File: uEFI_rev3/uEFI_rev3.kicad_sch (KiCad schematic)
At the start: 89 parts, among them J1 USB_B, J2 Tag connect, J4 Conn_02x08_Odd_Even, J5 Conn_01x03, Q11 SS8050, Q12 AO3400A, Q13 AO3400A, Q8 SS8050, Q9 SS8050, SW1 SW_Push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

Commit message: uEFI r3.2
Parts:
- added C42: 100uF ±20% 35V, Capacitor_SMD:CP_Elec_6.3x7.7, symbol Device:CP_Small
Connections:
- net +12V: now also C42.1
- net GND: now also C42.2
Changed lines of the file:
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@@
     (stroke (width 0) (type solid) (color 0 0 0 0))
   )
+  (wire (pts (xy 163.83 40.005) (xy 163.83 41.275))
+    (stroke (width 0) (type default) (color 0 0 0 0))
+  )
   (wire (pts (xy 60.96 26.67) (xy 75.565 26.67))
     (stroke (width 0) (type solid) (color 0 0 0 0))
@@
     (stroke (width 0) (type solid) (color 0 0 0 0))
   )
+  (wire (pts (xy 163.83 46.355) (xy 163.83 50.165))
+    (stroke (width 0) (type default) (color 0 0 0 0))
+  )
   (wire (pts (xy 185.42 224.79) (xy 185.42 227.33))
     (stroke (width 0) (type solid) (color 0 0 0 0))
@@
     (pin "2")
   )
+  (symbol (lib_id "power:GND") (at 163.83 50.165 0) (unit 1)
+    (in_bom yes) (on_board yes)
+    (property "Reference" "#PWR070" (id 0) (at 163.83 56.515 0)
+      (effects (font (size 1.27 1.27)) hide)
+    )
+    (property "Value" "GND" (id 1) (at 163.9443 54.4894 0))
+    (property "Footprint" "" (id 2) (at 163.83 50.165 0)
+      (effects (font (size 1.27 1.27)) hide)
+    )
+    (property "Datasheet" "" (id 3) (at 163.83 50.165 0)
+      (effects (font (size 1.27 1.27)) hide)
+    )
+    (pin "1")
+  )
   (symbol (lib_id "Device:LED") (at 374.015 201.93 90) (unit 1)
     (in_bom yes) (on_board yes)
@@
     (pin "2")
   )
+  (symbol (lib_id "Device:CP_Small") (at 163.83 43.815 0) (unit 1)
+    (in_bom yes) (on_board yes)
+    (property "Reference" "C42" (id 0) (at 166.0652 42.6466 0)
+      (effects (font (size 1.27 1.27)) (justify left))
+    )
+    (property "Value" "100uF ±20% 35V" (id 1) (at 166.0652 44.958 0)
+      (effects (font (size 1.27 1.27)) (justify left))
+    )
+    (property "Footprint" "Capacitor_SMD:CP_Elec_6.3x7.7" (id 2) (at 163.83 43.815 0)
+      (effects (font (size 1.27 1.27)) hide)
+    )
+    (property "Datasheet" "~" (id 3) (at 163.83 43.815 0)
+      (effects (font (size 1.27 1.27)) hide)
+    )
+    (property "LCSC" "C141427" (id 4) (at 163.83 43.815 0)
+      (effects (font (size 0.889 0.889)) hide)
+    )
+    (pin "1")
+    (pin "2")
+  )
   (symbol (lib_id "Device:LED") (at 372.745 158.115 90) (unit 1)
     (in_bom yes) (on_board yes)
@@
     (pin "2")
   )
+  (symbol (lib_id "power:+12V") (at 163.83 40.005 0) (unit 1)
+    (in_bom yes) (on_board yes)
+    (property "Reference" "#PWR059" (id 0) (at 163.83 43.815 0)
+      (effects (font (size 1.27 1.27)) hide)
+    )
+    (property "Value" "+12V" (id 1) (at 164.1983 35.6806 0))
+    (property "Footprint" "" (id 2) (at 163.83 40.005 0)
+      (effects (font (size 1.27 1.27)) hide)
+    )
+    (property "Datasheet" "" (id 3) (at 163.83 40.005 0)
+      (effects (font (size 1.27 1.27)) hide)
+    )
+    (pin "1")
+  )
   (symbol (lib_id "Connector:TestPoint") (at 321.31 206.375 0) (unit 1)
     (in_bom yes) (on_board yes)
@@
       (reference "#PWR058") (unit 1) (value "GND") (footprint "")
     )
+    (path "/6a695035-302a-4633-872f-d86fe3f64f9b"
+      (reference "#PWR059") (unit 1) (value "+12V") (footprint "")
+    )
     (path "/00000000-0000-0000-0000-00005f54b134/6f9e6eea-f1a5-4e59-a7b8-03098e367ddb"
       (reference "#PWR060") (unit 1) (value "+5C") (footprint "")
@@
       (reference "#PWR069") (unit 1) (value "GNDA") (footprint "")
     )
+    (path "/0df50f59-0981-4c75-9182-aabf7e291901"
+      (reference "#PWR070") (unit 1) (value "GND") (footprint "")
+    )
     (path "/00000000-0000-0000-0000-00005f54b134/33b6552b-ec9a-44b7-995a-5c278ca4a586"
       (reference "#PWR071") (unit 1) (value "+5C") (footprint "")
@@
       (reference "C41") (unit 1) (value "0.01uF") (footprint "Capacitor_SMD:C_0805_2012Metric")
     )
+    (path "/1feee1ca-03cf-42e2-a7c2-0e718be37bce"
+      (reference "C42") (unit 1) (value "100uF ±20% 35V") (footprint "Capacitor_SMD:CP_Elec_6.3x7.7")
+    )
     (path "/00000000-0000-0000-0000-00005f54b134/00000000-0000-0000-0000-00006090d894"
       (reference "C49") (unit 1) (value "240pF") (footprint "Capacitor_SMD:C_0603_1608Metric")
@@
     )
     (path "/00000000-0000-0000-0000-00005f54b134/36d4577c-93b8-425e-bae5-ab676247b4dd"
-      (reference "D15") (unit 1) (value "K26") (footprint "Diode_SMD:D_SOD-123F")
+      (reference "D15") (unit 1) (value "K26") (footprint "Diode_SMD:D_SOD-323")
     )
     (path "/00000000-0000-0000-0000-00005f54b134/43df4a53-5a75-4543-88d3-50cd7393567d"
-      (reference "D16") (unit 1) (value "K26") (footprint "Diode_SMD:D_SOD-123F")
+      (reference "D16") (unit 1) (value "K26") (footprint "Diode_SMD:D_SOD-323")
     )
     (path "/00000000-0000-0000-0000-00005f54b134/3e35f35b-de57-42a1-b66b-690d937f1fec"
-      (reference "D17") (unit 1) (value "K26") (footprint "Diode_SMD:D_SOD-123F")
+      (reference "D17") (unit 1) (value "K26") (footprint "Diode_SMD:D_SOD-323")
     )
     (path "/00000000-0000-0000-0000-00005f54b134/78a824b0-87dc-437f-a732-d014d3bc51a5"
-      (reference "D18") (unit 1) (value "K26") (footprint "Diode_SMD:D_SOD-123F")
+      (reference "D18") (unit 1) (value "K26") (footprint "Diode_SMD:D_SOD-323")
     )
     (path "/00000000-0000-0000-0000-00005f54b134/961d11cf-9d35-4dc0-aeb1-54327f99e8be"
-      (reference "D19") (unit 1) (value "K26") (footprint "Diode_SMD:D_SOD-123F")
+      (reference "D19") (unit 1) (value "K26") (footprint "Diode_SMD:D_SOD-323")
     )
     (path "/00000000-0000-0000-0000-00005f54b134/21de7dcb-5425-42bb-8c9a-3bfd52b7a51a"
-      (reference "D20") (unit 1) (value "K26") (footprint "Diode_SMD:D_SOD-123F")
+      (reference "D20") (unit 1) (value "K26") (footprint "Diode_SMD:D_SOD-323")
     )
     (path "/00000000-0000-0000-0000-00005f54b134/2b82281b-f421-4ecf-b0db-00934e89dd91"
-      (reference "D21") (unit 1) (value "K26") (footprint "Diode_SMD:D_SOD-123F")
+      (reference "D21") (unit 1) (value "K26") (footprint "Diode_SMD:D_SOD-323")
     )
     (path "/00000000-0000-0000-0000-00005f54b134/eaa007a4-c036-46e7-bd00-a1283bc87d20"
-      (reference "D22") (unit 1) (value "K26") (footprint "Diode_SMD:D_SOD-123F")
+      (reference "D22") (unit 1) (value "K26") (footprint "Diode_SMD:D_SOD-323")
     )
     (path "/00000000-0000-0000-0000-00005f54b134/8d3f1cc5-e6e3-4ecd-92fe-e11a349d591c"
-      (reference "D23") (unit 1) (value "K26") (footprint "Diode_SMD:D_SOD-123F")
+      (reference "D23") (unit 1) (value "K26") (footprint "Diode_SMD:D_SOD-323")
     )
     (path "/00000000-0000-0000-0000-00005f54b134/36ef3d3a-8f83-46bb-b29a-eea3c6d5118e"
-      (reference "D24") (unit 1) (value "K26") (footprint "Diode_SMD:D_SOD-123F")
+      (reference "D24") (unit 1) (value "K26") (footprint "Diode_SMD:D_SOD-323")
     )
     (path "/00000000-0000-0000-0000-00005f54b134/e82e2f0c-57f5-4439-8e3d-91cef29bd2c9"
-      (reference "D25") (unit 1) (value "K26") (footprint "Diode_SMD:D_SOD-123F")
+      (reference "D25") (unit 1) (value "K26") (footprint "Diode_SMD:D_SOD-323")
     )
     (path "/00000000-0000-0000-0000-00005f54b134/81a46c04-d71f-4df5-813e-004892d33c88"
-      (reference "D26") (unit 1) (value "K26") (footprint "Diode_SMD:D_SOD-123F")
+      (reference "D26") (unit 1) (value "K26") (footprint "Diode_SMD:D_SOD-323")
     )
     (path "/00000000-0000-0000-0000-00005f54b134/cdd5fa70-1ceb-4b29-a11e-53b81b7b46c1"
-      (reference "D27") (unit 1) (value "K26") (footprint "Diode_SMD:D_SOD-123F")
+      (reference "D27") (unit 1) (value "K26") (footprint "Diode_SMD:D_SOD-323")
     )
     (path "/00000000-0000-0000-0000-00005f54b134/10469210-faff-4618-8468-0de9fb7c59f8"
-      (reference "D28") (unit 1) (value "K26") (footprint "Diode_SMD:D_SOD-123F")
+      (reference "D28") (unit 1) (value "K26") (footprint "Diode_SMD:D_SOD-323")
     )
     (path "/00000000-0000-0000-0000-00005f54b134/2e71025c-185d-4e5d-83c0-a2bf07693edb"
-      (reference "D29") (unit 1) (value "K26") (footprint "Diode_SMD:D_SOD-123F")
+      (reference "D29") (unit 1) (value "K26") (footprint "Diode_SMD:D_SOD-323")
     )
     (path "/00000000-0000-0000-0000-00005f54b134/377a7c0e-81de-4ed3-897a-8cba059786d4"
-      (reference "D30") (unit 1) (value "K26") (footprint "Diode_SMD:D_SOD-123F")
+      (reference "D30") (unit 1) (value "K26") (footprint "Diode_SMD:D_SOD-323")
     )
     (path "/b1829a8d-2693-4ef4-b38b-2a2550c6ec35/1dc2fd4e-3b86-436b-a8b5-0a3a743fc6a4"

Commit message: uEFI rev 3.3
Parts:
- removed H10: MountingHole, MountingHole:MountingHole_2.2mm_M2_Pad, symbol Mechanical:MountingHole
- LOGO1: footprint Symbol:OSHW-Logo2_14.6x12mm_SilkScreen -> Symbol:OSHW-Logo2_9.8x8mm_SilkScreen
- SYM1: footprint Symbol:KiCad-Logo2_6mm_SilkScreen -> Symbol:KiCad-Logo2_5mm_SilkScreen
- U23: footprint OpenEFI-STM32F_rev3:DIP-16_598_ELL -> uEFI_Library:IC_DRV8825_STEPPER_MOTOR_DRIVER_CARRIER

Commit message: pre-production files, uEFI v3.4
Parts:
- removed C34: 4.7nF, Capacitor_SMD:C_0805_2012Metric, symbol Device:C_Small
- C2, C3: footprint Capacitor_SMD:C_0805_2012Metric -> Capacitor_SMD:C_0603_1608Metric
- R1, R28: value R_Small -> 120R; LCSC C205298 -> (none)
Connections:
- net AUX_IN_1: now also U3.91 (PB5); no longer U3.23 (PA0)
- net AUX_IN_2: now also U3.92 (PB6); no longer U3.24 (PA1)
- net AUX_IN_3: now also U3.93 (PB7); no longer U3.25 (PA2)
- net AUX_IN_4: now also U3.95 (PB8); no longer U3.26 (PA3)
- net MUX_A: now reaches U3.83 (PD2)
- net MUX_B: now reaches U3.84 (PD3)
- net MUX_C: now reaches U3.85 (PD4)
- new net MUX_OUT: U3.23 (PA0)
- no-connect marks 10 -> 6
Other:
- sheet Sensores ports: added MUX_A, MUX_B, MUX_C, MUX_OUT, OV_DET; removed ADC_CS, SPI2_MISO, SPI2_MOSI, SPI2_SCK

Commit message: fix bom output
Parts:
- C2, C3: footprint Capacitor_SMD:C_0603_1608Metric -> Capacitor_SMD:C_0805_2012Metric
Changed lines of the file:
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@@
     (property "Reference" "C3" (id 0) (at 21.59 34.29 90))
     (property "Value" "15pF" (id 1) (at 27.94 34.29 90))
-    (property "Footprint" "Capacitor_SMD:C_0603_1608Metric" (id 2) (at 24.13 33.02 0)
+    (property "Footprint" "Capacitor_SMD:C_0805_2012Metric" (id 2) (at 24.13 33.02 0)
       (effects (font (size 1.27 1.27)) hide)
     )
@@
     (property "Reference" "C2" (id 0) (at 21.59 21.59 90))
     (property "Value" "15pF" (id 1) (at 27.94 21.59 90))
-    (property "Footprint" "Capacitor_SMD:C_0603_1608Metric" (id 2) (at 24.13 22.86 0)
+    (property "Footprint" "Capacitor_SMD:C_0805_2012Metric" (id 2) (at 24.13 22.86 0)
       (effects (font (size 1.27 1.27)) hide)
     )
@@
     )
     (path "/00000000-0000-0000-0000-00005f600cb6"
-      (reference "C2") (unit 1) (value "15pF") (footprint "Capacitor_SMD:C_0603_1608Metric")
+      (reference "C2") (unit 1) (value "15pF") (footprint "Capacitor_SMD:C_0805_2012Metric")
     )
     (path "/00000000-0000-0000-0000-00005f600caf"
-      (reference "C3") (unit 1) (value "15pF") (footprint "Capacitor_SMD:C_0603_1608Metric")
+      (reference "C3") (unit 1) (value "15pF") (footprint "Capacitor_SMD:C_0805_2012Metric")
     )
     (path "/00000000-0000-0000-0000-00005f54b134/764be23b-571a-4dbd-a005-e145a99fe9a0"
@@
       (reference "R54") (unit 1) (value "10k") (footprint "Resistor_SMD:R_0603_1608Metric")
     )
+    (path "/00000000-0000-0000-0000-00005f54b134/c750d212-7fef-4b39-a38b-9ed94e6c1b26"
+      (reference "R55") (unit 1) (value "200R") (footprint "Resistor_SMD:R_0603_1608Metric")
+    )
     (path "/00000000-0000-0000-0000-00005f54b134/0a9bcb63-f62c-4c70-8df3-ac0e8ff32f51"
       (reference "R56") (unit 1) (value "470R") (footprint "Resistor_SMD:R_0603_1608Metric")
     )
     (path "/00000000-0000-0000-0000-00005f54b134/5a9381fe-2b2b-4437-8627-b05d8026d9df"
-      (reference "R57") (unit 1) (value "1k7") (footprint "Resistor_SMD:R_0603_1608Metric")
+      (reference "R57") (unit 1) (value "1k5") (footprint "Resistor_SMD:R_0603_1608Metric")
     )
     (path "/4d1c7d0d-0ce4-457a-9ac6-71610fbdc912"
@@
     )
     (path "/8d3d2293-e570-4555-b12b-74c389ae5124/8a8578e2-5aad-4309-8ef3-9385398ae4fb"
-      (reference "R121") (unit 1) (value "R_Small") (footprint "Resistor_SMD:R_0603_1608Metric")
+      (reference "R121") (unit 1) (value "10k") (footprint "Resistor_SMD:R_0603_1608Metric")
     )
     (path "/8d3d2293-e570-4555-b12b-74c389ae5124/ac97a1a7-3d68-44d4-913b-2b5fa7a47f1f"
-      (reference "R122") (unit 1) (value "R_Small") (footprint "Resistor_SMD:R_0603_1608Metric")
+      (reference "R122") (unit 1) (value "10k") (footprint "Resistor_SMD:R_0603_1608Metric")
     )
     (path "/00000000-0000-0000-0000-00005f6fa84a"

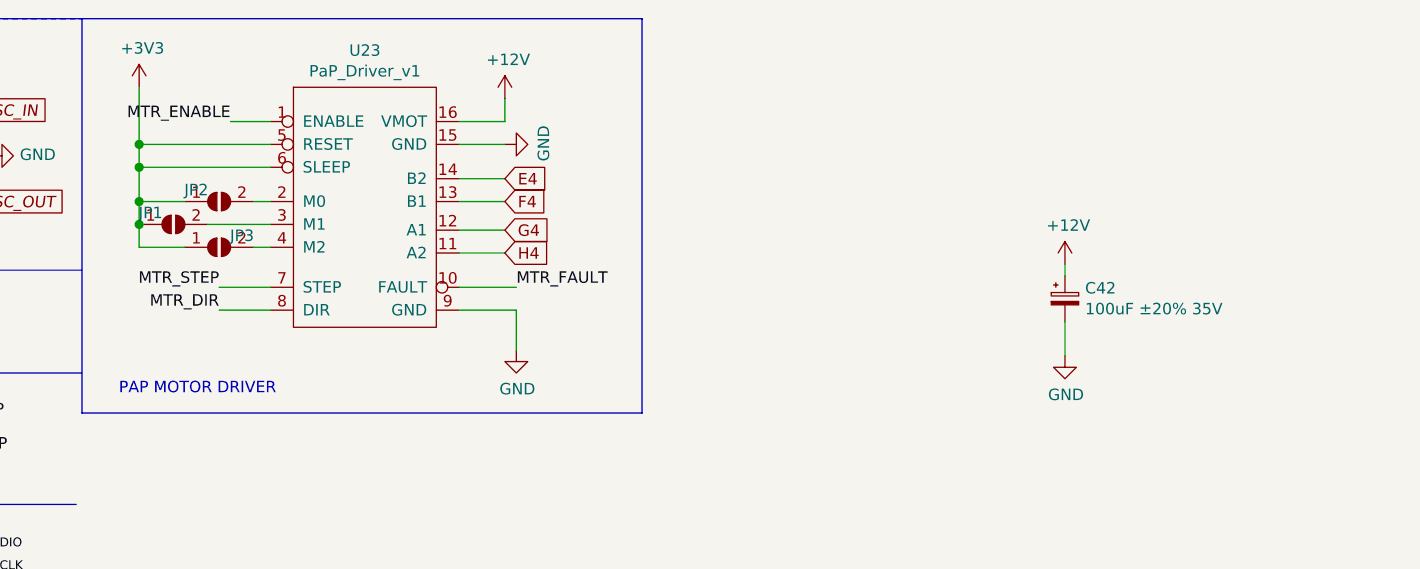
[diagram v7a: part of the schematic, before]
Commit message: uEFI v3, fix 12v => 5v overcurrent issue
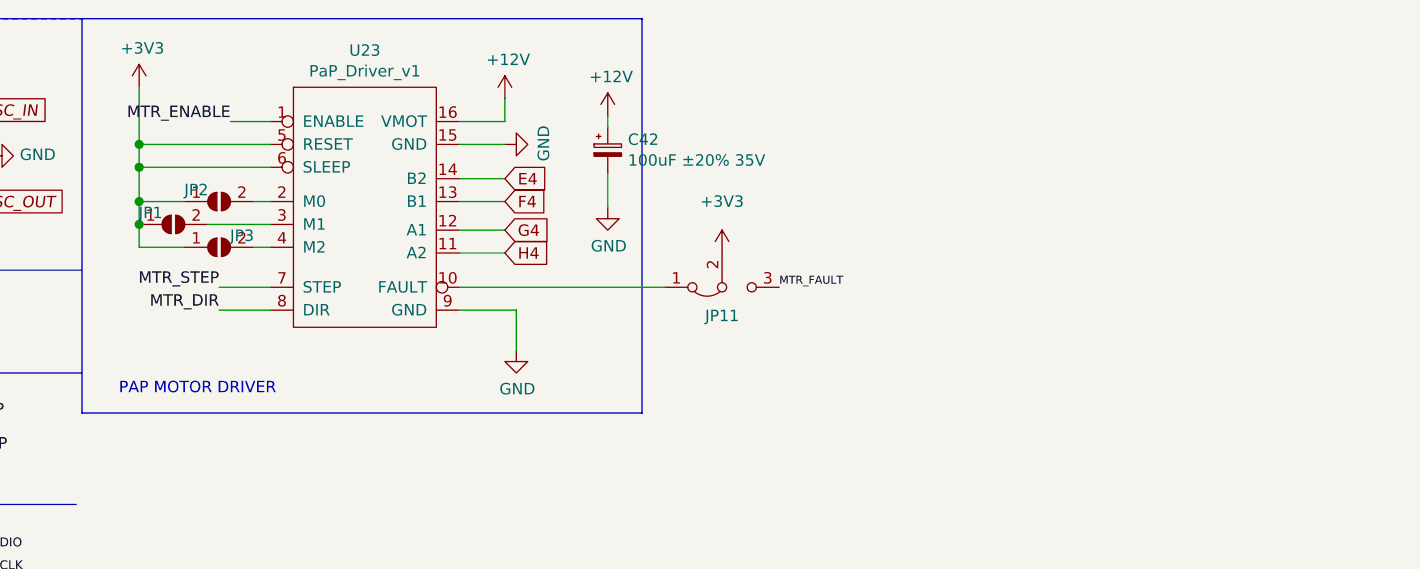
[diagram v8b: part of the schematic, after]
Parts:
- added JP11: ~, Jumper:SolderJumper-3_P1.3mm_Bridged2Bar12_Pad1.0x1.5mm_NumberLabels, symbol Jumper:Jumper_3_Bridged12
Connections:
- net +3V3: now also JP11.2 (C)
- net MTR_FAULT: now also JP11.3 (B); no longer U23.10 (FAULT)
- new net: JP11.1 (A), U23.10 (FAULT)
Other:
- moved on the sheet: C42
